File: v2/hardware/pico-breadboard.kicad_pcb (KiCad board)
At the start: 2 copper layers, 100 x 93 mm, 24 parts, among them J3 5V CONNECTOR, J4 GND CONNECTOR, J5 3.3V CONNECTOR, J6 Conn_01x20, J7 Conn_01x20, J8 SCREEN CONNECTOR, U1 Pico

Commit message: v2 updated
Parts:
- removed BUTTON1, BUTTON2: SW_SPST, Library:SW_PUSH_6mm
- removed TR1: BC517, Library:TO-92_Inline
- added FID1: Fiducial, Library:Fiducial_1mm_Mask2mm, F.Cu at (105.3, 129.4)
- added FID2: Fiducial, Library:Fiducial_1mm_Mask2mm, F.Cu at (176.8, 124.1)
- added FID3: Fiducial, Library:Fiducial_1mm_Mask2mm, F.Cu at (168.6, 38.4)
- added FID4: Fiducial, Library:Fiducial_1mm_Mask2mm, F.Cu at (100.9, 38.4)
- added G***: LOGO, Library:LOGO, B.Cu at (169.4, 86.9)
- added G***: LOGO, Library:LOGO, B.Cu at (129.7, 86.9)
- added H1: MountingHole, Library:MountingHole_3mm, B.Cu at (87.7, 36.9)
- added H2: MountingHole, Library:MountingHole_3mm, F.Cu at (181.7, 36.9)
- added H3: MountingHole, Library:MountingHole_3mm, F.Cu at (87.7, 129.8)
- added H4: MountingHole, Library:MountingHole_3mm, F.Cu at (181.7, 129.8)
- added J1: Conn_01x05, Library:PinHeader_1x05_P2.54mm_Vertical, F.Cu at (151.7, 98.0)
- added J10: MPU6050 CONNECTOR, Library:PinHeader_1x04_P2.54mm_Vertical, F.Cu at (120.4, 129.4)
- added J11: Conn_01x03, Library:PinHeader_1x03_P2.54mm_Vertical, F.Cu at (181.4, 65.0)
- added J12: Conn_01x03, Library:PinHeader_1x03_P2.54mm_Vertical, F.Cu at (97.8, 129.4)
- added J2: LED, Library:PinHeader_1x04_P2.54mm_Vertical, F.Cu at (158.1, 38.2)
- added J9: Conn_01x03, Library:PinHeader_1x03_P2.54mm_Vertical, F.Cu at (181.4, 45.5)
- added Q1: BC817, Library:SOT-23, F.Cu at (153.1, 119.7)
- added REF**: KiCad-Logo2_5mm_SilkScreen, Library:KiCad-Logo2_5mm_SilkScreen, B.Cu at (99.7, 70.5)
- added REF**: OSHW-Logo_11.4x12mm_SilkScreen, Library:OSHW-Logo_11.4x12mm_SilkScreen, B.Cu at (169.5, 69.5)
- added RV1: R_Potentiometer, Library:Potentiometer_Omeg_PC16BU_Horizontal, F.Cu at (182.2, 84.8)
- added SW1: SW_SPST, Library:SW_SPST_PTS810, F.Cu at (151.4, 128.9)
- added SW2: SW_SPST, Library:SW_SPST_PTS810, F.Cu at (163.4, 120.9)
- added SW3: SW_SPST, Library:SW_SPST_PTS810, F.Cu at (163.4, 128.9)
- added SW4: SW_SPST, Library:SW_SPST_PTS810, F.Cu at (175.4, 128.9)
- added SW5: RotaryEncoder_Switch_MP, Library:RotaryEncoder_Alps_EC11E-Switch_Vertical_H20mm, F.Cu at (174.1, 117.0)
- BZ1: footprint Library:Buzzer_15x7.5RM7.6 -> Library:Buzzer_12mm7.6
- J6: value Conn_01x20 -> Conn_01x12; footprint Library:PinHeader_1x20_P2.54mm_Vertical -> Library:PinHeader_1x12_P2.54mm_Vertical
- J7: value Conn_01x20 -> Conn_01x11; footprint Library:PinHeader_1x20_P2.54mm_Vertical -> Library:PinHeader_1x11_P2.54mm_Vertical
- LED1, LED2, LED3, LED4: footprint Library:LED_D5.0mm -> Library:LED_0603_1608Metric
- R1, R2, R3, R4, R9: footprint Library:R_Axial_DIN0204_L3.6mm_D1.6mm_P7.62mm_Horizontal -> Library:R_0402_1005Metric
- moved J6 95.5 mm to (110.5, 38.2)
- moved J8 55.6 mm to (131.6, 129.3), turned to 90 degrees
- moved R4 36.4 mm to (145.3, 120.3)
- moved LED4 36.3 mm to (142.9, 123.8)
- moved R9 26.3 mm to (152.1, 123.5), turned to 90 degrees
- moved R3 25.8 mm to (145.3, 113.3)
- moved LED3 23.8 mm to (142.9, 116.8)
- moved J7 22.9 mm to (109.9, 97.8)
- moved R1 22.5 mm to (145.1, 99.3)
- moved R2 19.8 mm to (145.3, 106.3)
- moved LED1 15.0 mm to (142.9, 102.8)
- moved LED2 14.2 mm to (142.9, 109.8)
- moved U2 6.00 mm to (92.7, 40.9)
- moved G*** 4.35 mm to (99.6, 86.9)
- moved BZ1 4.14 mm to (161.8, 107.8)
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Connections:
- net Net-(J6-Pin_1) renamed /GPIO0
- net Net-(J6-Pin_2) renamed /GPIO1
- J6 pad 10: Net-(J6-Pin_10) -> /GPIO10
- J6 pad 11: Net-(J6-Pin_11) -> /GPIO11
- J6 pad 12: Net-(J6-Pin_12) -> /GPIO12
- J6 pad 3: GND -> /GPIO2
- J6 pad 4: Net-(J6-Pin_4) -> /GPIO3
- J6 pad 5: Net-(J6-Pin_5) -> /GPIO4
- J6 pad 6: Net-(J6-Pin_6) -> /GPIO5
- J6 pad 7: Net-(J6-Pin_7) -> /GPIO6
- J6 pad 8: GND -> /GPIO7
- J6 pad 9: Net-(J6-Pin_9) -> /GPIO8
- J7 pad 1: +5V -> /GPIO28
- J7 pad 10: Net-(J7-Pin_10) -> /GPIO16
- J7 pad 11: Net-(J7-Pin_11) -> /GPIO13
- J7 pad 2: Net-(J7-Pin_2) -> /GPIO27
- J7 pad 3: GND -> /GPIO26
- J7 pad 4: Net-(J7-Pin_4) -> /GPIO22
- J7 pad 5: +3.3V -> /GPIO21
- J7 pad 6: Net-(J7-Pin_6) -> /GPIO20
- J7 pad 7: Net-(J7-Pin_7) -> /GPIO19
- J7 pad 8: GND -> /GPIO18
- J7 pad 9: Net-(J7-Pin_9) -> /GPIO17
- J8 pad 1: /SDA -> GND
- J8 pad 2: /SCL -> +3.3V
- J8 pad 3: +3.3V -> /GPIO13
- J8 pad 4: GND -> /GPIO12
- U1 pad 10: Net-(J6-Pin_10) -> /GPIO7
- U1 pad 11: Net-(J6-Pin_11) -> /GPIO8
- U1 pad 12: Net-(J6-Pin_12) -> /BUZZER
- U1 pad 14: Net-(J6-Pin_14) -> /GPIO10
- U1 pad 15: Net-(J6-Pin_15) -> /GPIO11
- U1 pad 16: /SW2 -> /GPIO12
- U1 pad 17: /SW1 -> /GPIO13
- U1 pad 19: /LED1 -> /A
- U1 pad 20: /LED2 -> /B
- U1 pad 21: /LED3 -> /GPIO16
- U1 pad 22: /LED4 -> /GPIO17
- U1 pad 24: /BUZZER -> /GPIO18
- U1 pad 25: Net-(J7-Pin_16) -> /GPIO19
- U1 pad 26: /SDA -> /GPIO20
- U1 pad 27: /SCL -> /GPIO21
- U1 pad 29: Net-(J7-Pin_12) -> /GPIO22
- U1 pad 30: Net-(J7-Pin_11) -> unconnected-(U1-RUN-Pad30)
- U1 pad 31: Net-(J7-Pin_10) -> /GPIO26
- U1 pad 32: Net-(J7-Pin_9) -> /GPIO27
- U1 pad 34: Net-(J7-Pin_7) -> /GPIO28
- U1 pad 35: Net-(J7-Pin_6) -> unconnected-(U1-ADC_VREF-Pad35)
- U1 pad 37: Net-(J7-Pin_4) -> unconnected-(U1-3V3_EN-Pad37)
- U1 pad 39: Net-(J7-Pin_2) -> +5V
- U1 pad 4: Net-(J6-Pin_4) -> /GPIO2
- U1 pad 40: +5V -> unconnected-(U1-VBUS-Pad40)
- U1 pad 5: Net-(J6-Pin_5) -> /GPIO3
- U1 pad 6: Net-(J6-Pin_6) -> /GPIO4
- U1 pad 7: Net-(J6-Pin_7) -> /GPIO5
- U1 pad 9: Net-(J6-Pin_9) -> /GPIO6
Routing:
- net /GPIO10: track 0.00 -> 151.7 mm, vias 0 -> 1
- net /GPIO11: track 0.00 -> 151.7 mm, vias 0 -> 1
- net +5V: track 155.2 -> 303.5 mm
- net /GPIO12: track 0.00 -> 124.7 mm
- net /GPIO0: track 7.62 -> 106.3 mm
- net /GPIO3: track 0.00 -> 93.8 mm
- net /GPIO6: track 0.00 -> 93.7 mm
- net /GPIO7: track 0.00 -> 93.7 mm
- net /GPIO4: track 0.00 -> 93.7 mm
- net /GPIO2: track 0.00 -> 93.7 mm
- net /GPIO5: track 0.00 -> 93.7 mm
- net /GPIO8: track 0.00 -> 92.6 mm
- net /GPIO1: track 7.62 -> 94.7 mm
- net /GPIO26: track 0.00 -> 84.1 mm, vias 0 -> 1
- net /SCL: track 80.2 -> 0.00 mm
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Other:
- board size 100 x 93 mm -> 100 x 99 mm
- board text added: "1"
- board text added: "2"
- board text added: "3"
- board text added: "4"
- board text added: "5"
- board text added: "BUTTON"
- board text added: "D"
- board text added: "ENCODER"
- board text added: "GP10"
- board text added: "GP11"
- board text added: "IMU"
- board text added: "LED"
- board text added: "NEOPIXEL"
- board text added: "SERVO1"
- board text added: "SERVO2"
- board text added: "designed by"
- board text removed: "Designed by RS for ME110"

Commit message: update
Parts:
- removed the G*** at (99.6, 86.9)
- added G***: LOGO, LOGO, B.Cu at (92.7, 87.1)
- added G***: LOGO, LOGO, B.Cu at (150.4, 88.6)
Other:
- board text added: "sponsored by"

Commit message: update
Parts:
- G***: footprint LOGO -> Library:LOGO
- U2: value ~ -> BREADBOARD
- moved G*** 72.1 mm to (162.4, 68.8)
- moved REF** 71.9 mm to (99.7, 86.9)
- moved G*** 54.1 mm to (99.7, 69.8)
- moved REF** 29.2 mm to (123.8, 86.8)
- moved G*** 16.5 mm to (146.2, 86.9)

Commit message: update
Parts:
- G***: footprint LOGO -> Library:LOGO
- moved G*** 1.25 mm to (144.9, 86.9)
- moved REF** 1.19 mm to (122.7, 86.8)

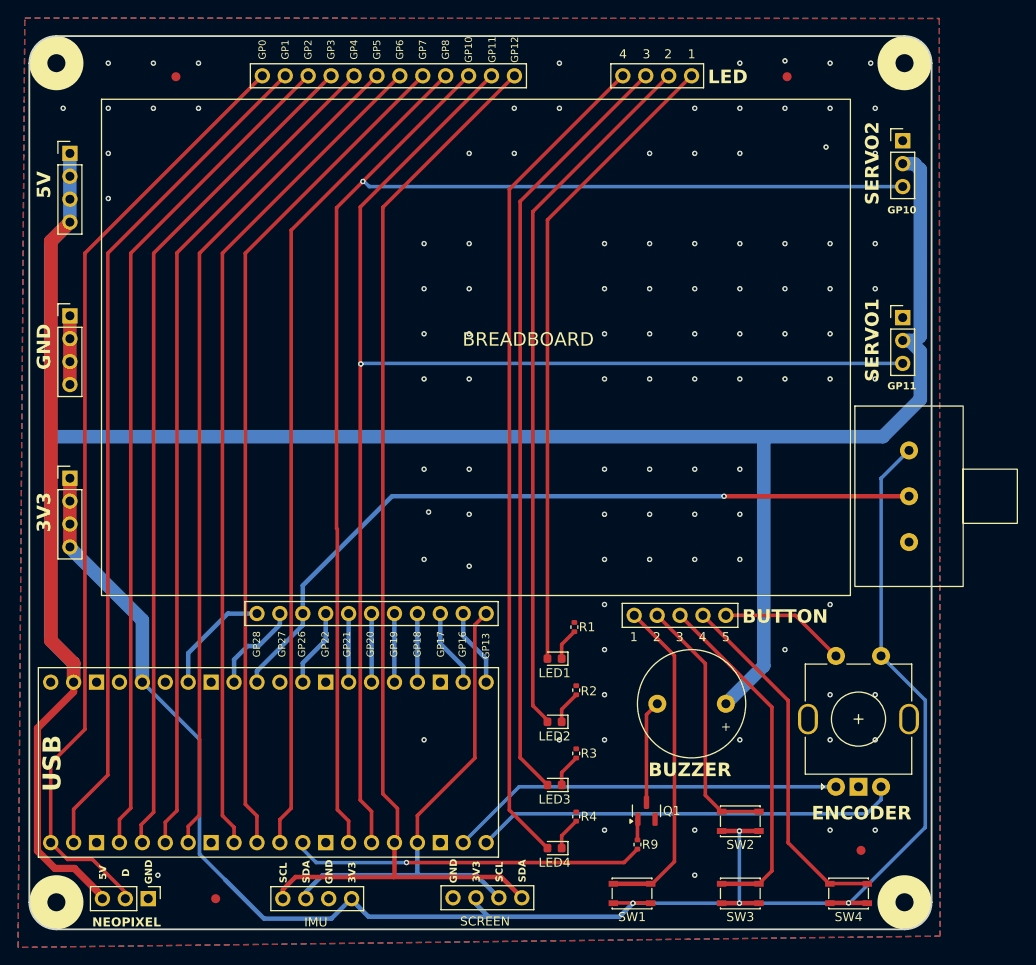
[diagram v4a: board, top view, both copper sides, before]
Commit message: silkscreen fixel board size adjusted
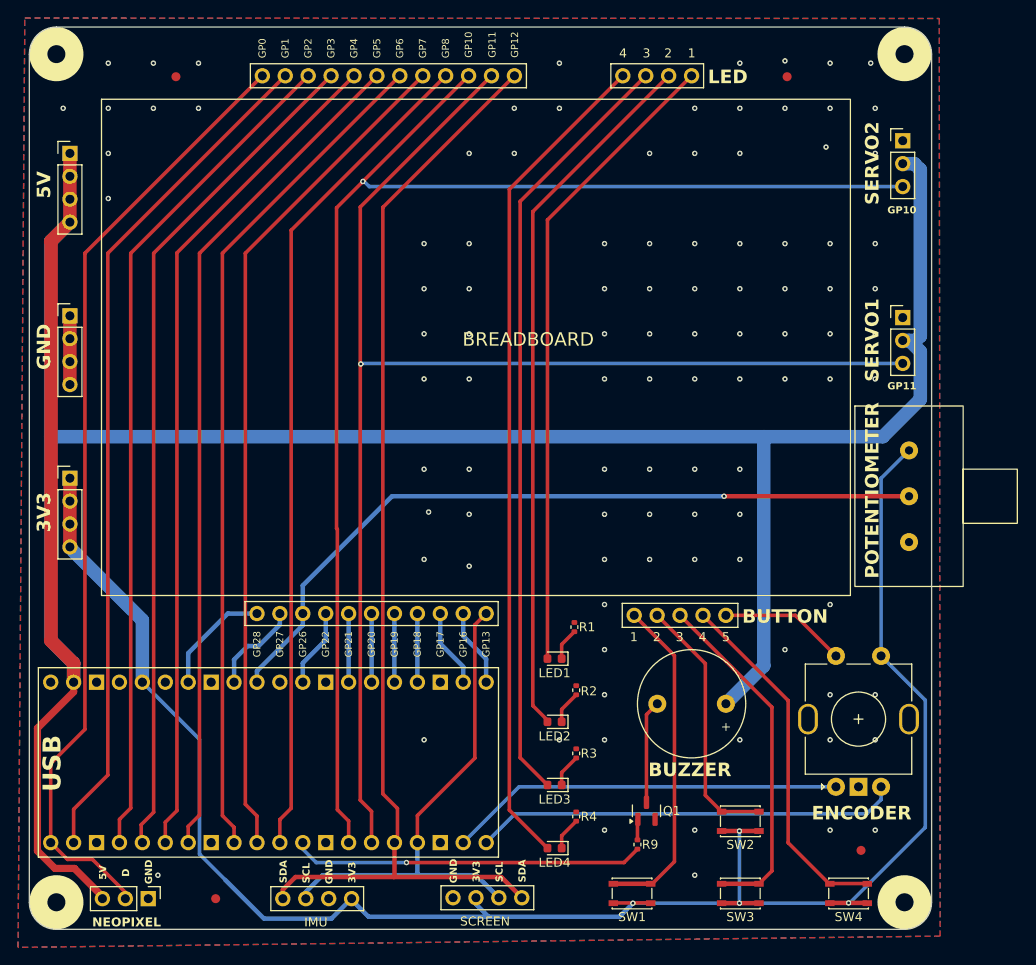
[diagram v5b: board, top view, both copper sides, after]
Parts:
- moved H1 1.00 mm to (87.7, 35.9)
- moved H2 1.00 mm to (181.7, 35.9)
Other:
- board size 100 x 99 mm -> 100 x 100 mm
- board text added: "POTENTIOMETER"

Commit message: minor changes
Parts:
- added J13: Polarity Select, Connector_PinHeader_2.54mm:PinHeader_2x02_P2.54mm_Vertical, F.Cu at (127.3, 127.8)
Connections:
- J8 pad 1: GND -> /T1
- J8 pad 2: +3.3V -> /T2
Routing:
- net /T2: track 0.00 -> 8.94 mm
- net /T1: track 0.00 -> 7.57 mm
- net /GPIO13: track 56.1 -> 56.6 mm
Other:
- board text added: "T1"
- board text added: "T2"
